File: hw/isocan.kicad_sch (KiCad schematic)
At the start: 14 parts, among them U9 ADM3053BRW_C579192

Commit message: WIP XT30?
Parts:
- FB1, FB2: footprint PCM_Ferrite_SMD_AKL:Ferrite_0402_1005Metric -> Resistor_SMD:R_0402_1005Metric
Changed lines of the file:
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@@
       (effects (font (size 1.27 1.27)))
     )
-    (property "Footprint" "PCM_Ferrite_SMD_AKL:Ferrite_0402_1005Metric" (at 180.467 111.633 90)
+    (property "Footprint" "Resistor_SMD:R_0402_1005Metric" (at 180.467 111.633 90)
       (effects (font (size 1.27 1.27)) hide)
     )
@@
       (effects (font (size 1.27 1.27)))
     )
-    (property "Footprint" "PCM_Ferrite_SMD_AKL:Ferrite_0402_1005Metric" (at 180.467 98.298 90)
+    (property "Footprint" "Resistor_SMD:R_0402_1005Metric" (at 180.467 98.298 90)
       (effects (font (size 1.27 1.27)) hide)
     )

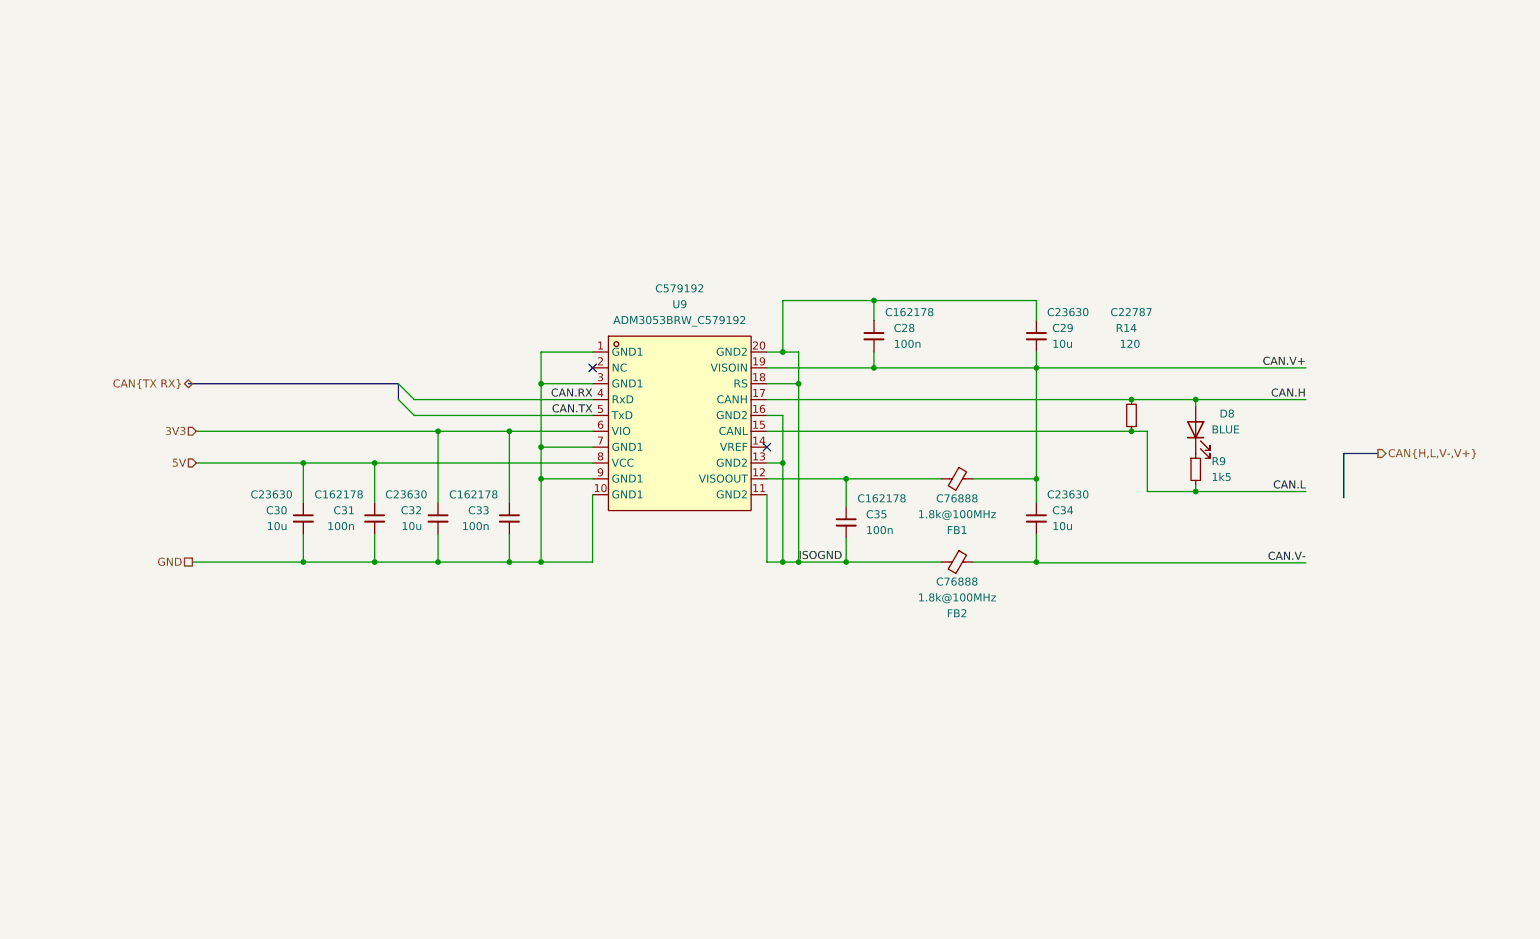
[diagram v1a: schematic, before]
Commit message: [Hw] compact discrete 4 wire iso can, approx drv routing, eeprom
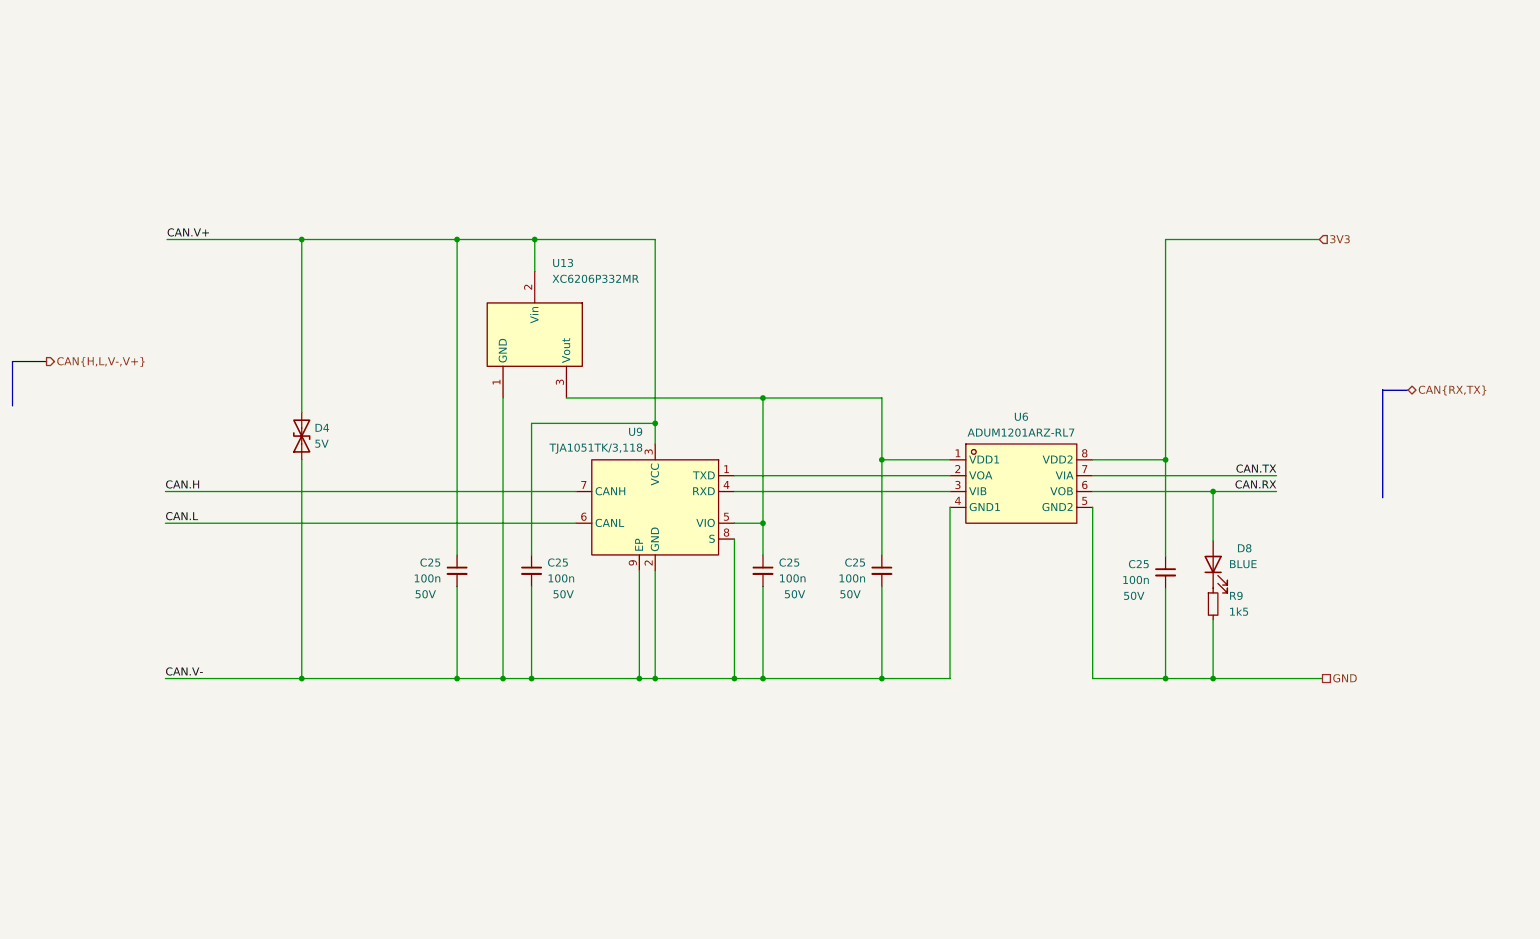
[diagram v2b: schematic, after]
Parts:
- removed C28, C31, C33, C35: 100n, Capacitor_SMD:C_0402_1005Metric, symbol Device:C_Small
- removed C29, C30, C32, C34: 10u, Capacitor_SMD:C_0603_1608Metric, symbol Device:C_Small
- removed FB1, FB2: 1.8k@100MHz, Resistor_SMD:R_0402_1005Metric, symbol Device:FerriteBead_Small
- removed R14: 120, Resistor_SMD:R_0603_1608Metric, symbol Device:R_Small
- removed U9: ADM3053BRW_C579192, easyeda:SO-20_L12.8-W7.5-P1.27-LS10.3-BL, symbol easyeda:ADM3053BRW_C579192
- added C25 (x5): 100n, Capacitor_SMD:C_0402_1005Metric, symbol Device:C_Small
- added D4: 5V, Diode_SMD:D_0603_1608Metric, symbol Device:D_TVS
- added U13: XC6206P332MR, easyeda:SOT-23-3_L2.9-W1.6-P1.90-LS2.8-BR, symbol easyeda:XC6206P332MR
- added U6: ADUM1201ARZ-RL7, easyeda:SOIC-8_L4.9-W3.9-P1.27-LS6.0-BL, symbol easyeda:ADUM1201ARZ-RL7
- added U9: TJA1051TK/3,118, easyeda:HVSON-8_L3.0-W3.0-P0.65-BL-EP, symbol easyeda:TJA1051TK_3,118
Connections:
- net 3V3: now also C25.1, U6.8 (VDD2)
- net CAN.H: now also U9.7 (CANH); no longer D8.2 (A)
- net CAN.L: now also U9.6 (CANL); no longer R9.2
- net CAN.RX: now also D8.2 (A), U6.6 (VOB)
- net CAN.TX: now also U6.7 (VIA)
- net CAN.V+: now also C25.1, C25.1, D4.2 (A2), U13.2 (Vin), U9.3 (VCC)
- net CAN.V-: now also C25.2, C25.2, C25.2, C25.2, D4.1 (A1), U13.1 (GND), U6.4 (GND1), U9.2 (GND), U9.8 (S), U9.9 (EP)
- net GND: now also R9.2, C25.2, U6.5 (GND2)
- new net: C25.1, C25.1, U13.3 (Vout), U6.1 (VDD1), U9.5 (VIO)
- new net: U6.2 (VOA), U9.1 (TXD)
- new net: U6.3 (VIB), U9.4 (RXD)
- no-connect marks 2 -> 0
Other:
- moved on the sheet: D8, R9

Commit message: [Hw] Tiny eeprom, all components fit on board!
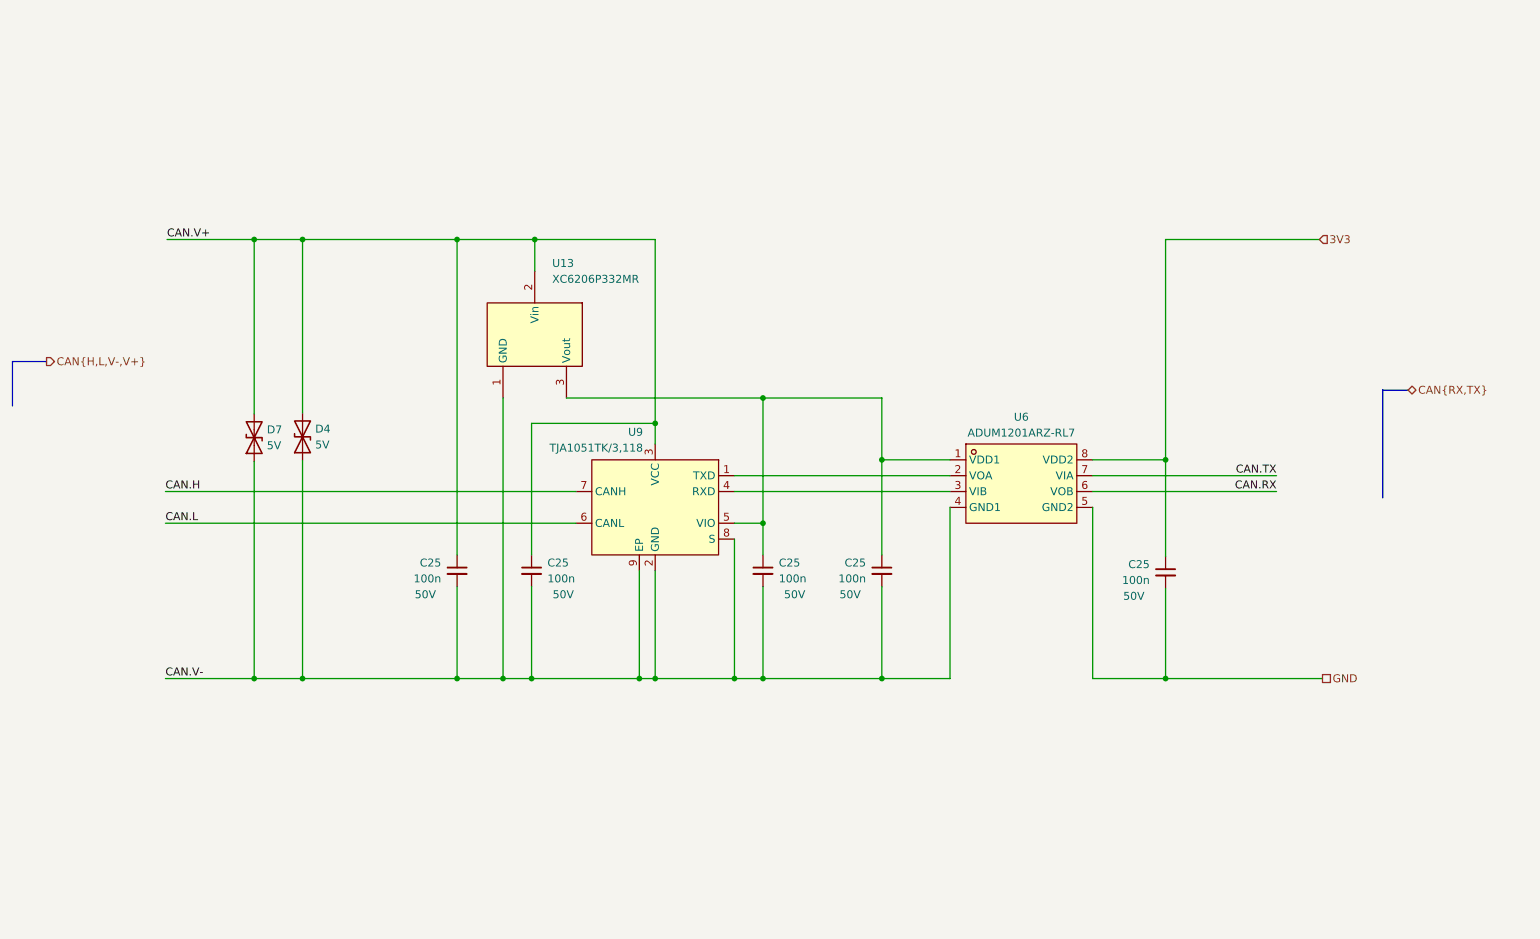
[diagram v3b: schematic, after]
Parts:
- removed D8: BLUE, LED_SMD:LED_0603_1608Metric, symbol Device:LED
- removed R9: 1k5, Resistor_SMD:R_0603_1608Metric, symbol Device:R_Small
- added D7: 5V, easyeda:X1-DFN1006-2_L1.0-W0.6-RD, symbol Device:D_TVS
- D4: footprint Diode_SMD:D_0603_1608Metric -> easyeda:X1-DFN1006-2_L1.0-W0.6-RD; LCSC C316054 -> C316041
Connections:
- net CAN.V+: now also D7.2 (A2)
- net CAN.V-: now also D7.1 (A1)
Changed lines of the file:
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@@
   (junction (at 149.352 132.08) (diameter 0) (color 0 0 0 0)
   )
+  (junction (at 75.565 61.722) (diameter 0) (color 0 0 0 0)
+  )
   (junction (at 129.54 132.08) (diameter 0) (color 0 0 0 0)
   )
@@
   (junction (at 168.402 132.08) (diameter 0) (color 0 0 0 0)
   )
-  (junction (at 75.438 132.08) (diameter 0) (color 0 0 0 0)
-  )
-  (junction (at 75.438 61.722) (diameter 0) (color 0 0 0 0)
-  )
-  (junction (at 221.488 132.08) (diameter 0) (color 0 0 0 0)
-  )
   (junction (at 149.352 87.122) (diameter 0) (color 0 0 0 0)
   )
@@
   (junction (at 112.268 132.08) (diameter 0) (color 0 0 0 0)
   )
+  (junction (at 67.818 61.722) (diameter 0) (color 0 0 0 0)
+  )
   (junction (at 112.776 61.722) (diameter 0) (color 0 0 0 0)
   )
+  (junction (at 75.565 132.08) (diameter 0) (color 0 0 0 0)
+  )
   (junction (at 213.868 132.08) (diameter 0) (color 0 0 0 0)
   )
   (junction (at 100.33 61.722) (diameter 0) (color 0 0 0 0)
   )
-  (junction (at 221.488 102.108) (diameter 0) (color 0 0 0 0)
-  )
   (junction (at 144.78 132.08) (diameter 0) (color 0 0 0 0)
   )
-  (wire (pts (xy 75.438 132.08) (xy 100.33 132.08))
-    (stroke (width 0) (type default))
+  (junction (at 67.818 132.08) (diameter 0) (color 0 0 0 0)
   )
   (wire (pts (xy 100.33 132.08) (xy 107.696 132.08))
     (stroke (width 0) (type default))
   )
+  (wire (pts (xy 75.565 132.08) (xy 100.33 132.08))
+    (stroke (width 0) (type default))
+  )
   (wire (pts (xy 144.78 99.568) (xy 179.324 99.568))
     (stroke (width 0) (type default))
   )
+  (wire (pts (xy 75.565 61.722) (xy 100.33 61.722))
+    (stroke (width 0) (type default))
+  )
   (wire (pts (xy 168.402 87.122) (xy 168.402 97.028))
     (stroke (width 0) (type default))
@@
     (stroke (width 0) (type default))
   )
-  (wire (pts (xy 213.868 132.08) (xy 221.488 132.08))
+  (wire (pts (xy 213.868 132.08) (xy 239.014 132.08))
     (stroke (width 0) (type default))
   )
@@
     (stroke (width 0) (type default))
   )
-  (wire (pts (xy 53.848 61.722) (xy 75.438 61.722))
-    (stroke (width 0) (type default))
-  )
-  (wire (pts (xy 221.488 102.108) (xy 231.648 102.108))
+  (wire (pts (xy 53.848 61.722) (xy 67.818 61.722))
     (stroke (width 0) (type default))
   )
@@
     (stroke (width 0) (type default))
   )
+  (wire (pts (xy 67.818 97.282) (xy 67.818 132.08))
+    (stroke (width 0) (type default))
+  )
   (wire (pts (xy 202.184 132.08) (xy 213.868 132.08))
     (stroke (width 0) (type default))
@@
     (stroke (width 0) (type default))
   )
-  (wire (pts (xy 75.438 97.028) (xy 75.438 132.08))
+  (wire (pts (xy 75.565 97.155) (xy 75.565 132.08))
     (stroke (width 0) (type default))
   )
@@
     (stroke (width 0) (type default))
   )
-  (wire (pts (xy 221.488 122.682) (xy 221.488 132.08))
+  (wire (pts (xy 67.818 61.722) (xy 67.818 89.662))
     (stroke (width 0) (type default))
   )
@@
     (stroke (width 0) (type default))
   )
-  (wire (pts (xy 75.438 61.722) (xy 75.438 89.408))
-    (stroke (width 0) (type default))
-  )
   (wire (pts (xy 179.324 132.08) (xy 179.324 104.648))
     (stroke (width 0) (type default))
@@
     (stroke (width 0) (type default))
   )
-  (wire (pts (xy 202.184 102.108) (xy 221.488 102.108))
+  (wire (pts (xy 202.184 102.108) (xy 231.648 102.108))
     (stroke (width 0) (type default))
   )
@@
     (stroke (width 0) (type default))
   )
-  (wire (pts (xy 53.594 132.08) (xy 75.438 132.08))
+  (wire (pts (xy 53.594 132.08) (xy 67.818 132.08))
     (stroke (width 0) (type default))
   )
@@
     (stroke (width 0) (type default))
   )
-  (wire (pts (xy 221.488 132.08) (xy 239.014 132.08))
-    (stroke (width 0) (type default))
-  )
   (wire (pts (xy 100.33 61.722) (xy 112.776 61.722))
     (stroke (width 0) (type default))
@@
     (stroke (width 0) (type default))
   )
-  (wire (pts (xy 221.488 109.982) (xy 221.488 102.108))
+  (wire (pts (xy 75.565 61.722) (xy 75.565 89.535))
     (stroke (width 0) (type default))
   )
@@
     (stroke (width 0) (type default))
   )
-  (wire (pts (xy 75.438 61.722) (xy 100.33 61.722))
+  (wire (pts (xy 67.818 132.08) (xy 75.565 132.08))
+    (stroke (width 0) (type default))
+  )
+  (wire (pts (xy 67.818 61.722) (xy 75.565 61.722))
     (stroke (width 0) (type default))
   )
@@
   )
   (wire (pts (xy 132.08 114.808) (xy 132.08 132.08))
+    (stroke (width 0) (type default))
+  )
+  (wire (pts (xy 75.565 132.207) (xy 75.565 132.08))
     (stroke (width 0) (type default))
   )
@@
     )
   )
-  (symbol (lib_id "Device:LED") (at 221.488 113.792 90) (unit 1)
-    (in_bom yes) (on_board yes) (dnp no)
-    (property "Reference" "D8" (at 225.298 111.252 90)
+  (symbol (lib_id "Device:D_TVS") (at 67.818 93.472 90) (unit 1)
+    (in_bom yes) (on_board yes) (dnp no) (fields_autoplaced)
+    (property "Reference" "D7" (at 69.85 92.202 90)
       (effects (font (size 1.27 1.27)) (justify right))
     )
-    (property "Value" "BLUE" (at 224.028 113.792 90)
+    (property "Value" "5V" (at 69.85 94.742 90)
       (effects (font (size 1.27 1.27)) (justify right))
     )
-    (property "Footprint" "LED_SMD:LED_0603_1608Metric" (at 221.488 113.792 0)
-      (effects (font (size 1.27 1.27)) hide)
-    )
-    (property "Datasheet" "~" (at 221.488 113.792 0)
-      (effects (font (size 1.27 1.27)) hide)
-    )
-    (property "LCSC" "C19189746" (at 221.488 113.792 90)
-      (effects (font (size 1.27 1.27)) hide)
-    )
-    (pin "1")
-    (pin "2")
-    (instances
-      (project "smart_servo"
-        (path "/3d5cfc11-2b2d-4555-a7d7-dadab43e84fa"
-          (reference "D8") (unit 1)
-        )
-      )
-      (project "foc8313"
-        (path "/6a0f293a-1ae1-497a-a3c1-0d8f9e6f81b9"
-          (reference "D4") (unit 1)
-        )
-        (path "/6a0f293a-1ae1-497a-a3c1-0d8f9e6f81b9/67c38edc-7843-4b4c-b50a-94fd700c0fa2"
-          (reference "D8") (unit 1)
-        )
-      )
-    )
-  )
-  (symbol (lib_id "Device:D_TVS") (at 75.438 93.218 90) (unit 1)
+    (property "Footprint" "easyeda:X1-DFN1006-2_L1.0-W0.6-RD" (at 67.818 93.472 0)
+      (effects (font (size 1.27 1.27)) hide)
+    )
+    (property "Datasheet" "~" (at 67.818 93.472 0)
+      (effects (font (size 1.27 1.27)) hide)
+    )
+    (property "LCSC" "C316041" (at 67.818 93.472 90)
+      (effects (font (size 1.27 1.27)) hide)
+    )
+    (pin "1")
+    (pin "2")
+    (instances
+      (project "foc8313"
+        (path "/6a0f293a-1ae1-497a-a3c1-0d8f9e6f81b9/67c38edc-7843-4b4c-b50a-94fd700c0fa2"
+          (reference "D7") (unit 1)
+        )
+      )
+    )
+  )
+  (symbol (lib_id "Device:D_TVS") (at 75.565 93.345 90) (unit 1)
     (in_bom yes) (on_board yes) (dnp no) (fields_autoplaced)
-    (property "Reference" "D4" (at 77.47 91.948 90)
+    (property "Reference" "D4" (at 77.597 92.075 90)
       (effects (font (size 1.27 1.27)) (justify right))
     )
-    (property "Value" "5V" (at 77.47 94.488 90)
+    (property "Value" "5V" (at 77.597 94.615 90)
       (effects (font (size 1.27 1.27)) (justify right))
     )
-    (property "Footprint" "Diode_SMD:D_0603_1608Metric" (at 75.438 93.218 0)
-      (effects (font (size 1.27 1.27)) hide)
-    )
-    (property "Datasheet" "~" (at 75.438 93.218 0)
-      (effects (font (size 1.27 1.27)) hide)
-    )
-    (property "LCSC" "C316054" (at 75.438 93.218 90)
+    (property "Footprint" "easyeda:X1-DFN1006-2_L1.0-W0.6-RD" (at 75.565 93.345 0)
+      (effects (font (size 1.27 1.27)) hide)
+    )
+    (property "Datasheet" "~" (at 75.565 93.345 0)
+      (effects (font (size 1.27 1.27)) hide)
+    )
+    (property "LCSC" "C316041" (at 75.565 93.345 90)
       (effects (font (size 1.27 1.27)) hide)
     )
@@
         )
       )
-    )
-  )
-  (symbol (lib_id "Device:R_Small") (at 221.488 120.142 0) (unit 1)
-    (in_bom yes) (on_board yes) (dnp no) (fields_autoplaced)
-    (property "Reference" "R9" (at 224.028 118.872 0)
-      (effects (font (size 1.27 1.27)) (justify left))
-    )
-    (property "Value" "1k5" (at 224.028 121.412 0)
-      (effects (font (size 1.27 1.27)) (justify left))
-    )
-    (property "Footprint" "Resistor_SMD:R_0603_1608Metric" (at 221.488 120.142 0)
-      (effects (font (size 1.27 1.27)) hide)
-    )
-    (property "Datasheet" "~" (at 221.488 120.142 0)
-      (effects (font (size 1.27 1.27)) hide)
-    )
-    (property "LCSC" "C22843" (at 221.488 120.142 0)
-      (effects (font (size 1.27 1.27)) hide)
-    )
-    (pin "1")
-    (pin "2")
-    (instances
-      (project "foc8313"
-        (path "/6a0f293a-1ae1-497a-a3c1-0d8f9e6f81b9"
-          (reference "R9") (unit 1)
-        )
-        (path "/6a0f293a-1ae1-497a-a3c1-0d8f9e6f81b9/67c38edc-7843-4b4c-b50a-94fd700c0fa2"
-          (reference "R9") (unit 1)
-        )
-      )
